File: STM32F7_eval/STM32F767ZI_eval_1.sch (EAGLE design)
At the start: 91 parts, among them CN1 GROVE-4P-CONN-I2C-90D, CN2 GROVE-4P-CONN-I2C-90D, CN3 GROVE-4P-CONN-I2C-90D, CN4 GROVE-4P-CONN-AN01-90D, CN5 ARDUINO_COMPAT_IF, CN6 STLINKV21_SWD_IF, CN7 WFT0750CZ09-SMD_, CN8 MCO_IF, CN9 UART_IF, Q1 PMF370XN_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

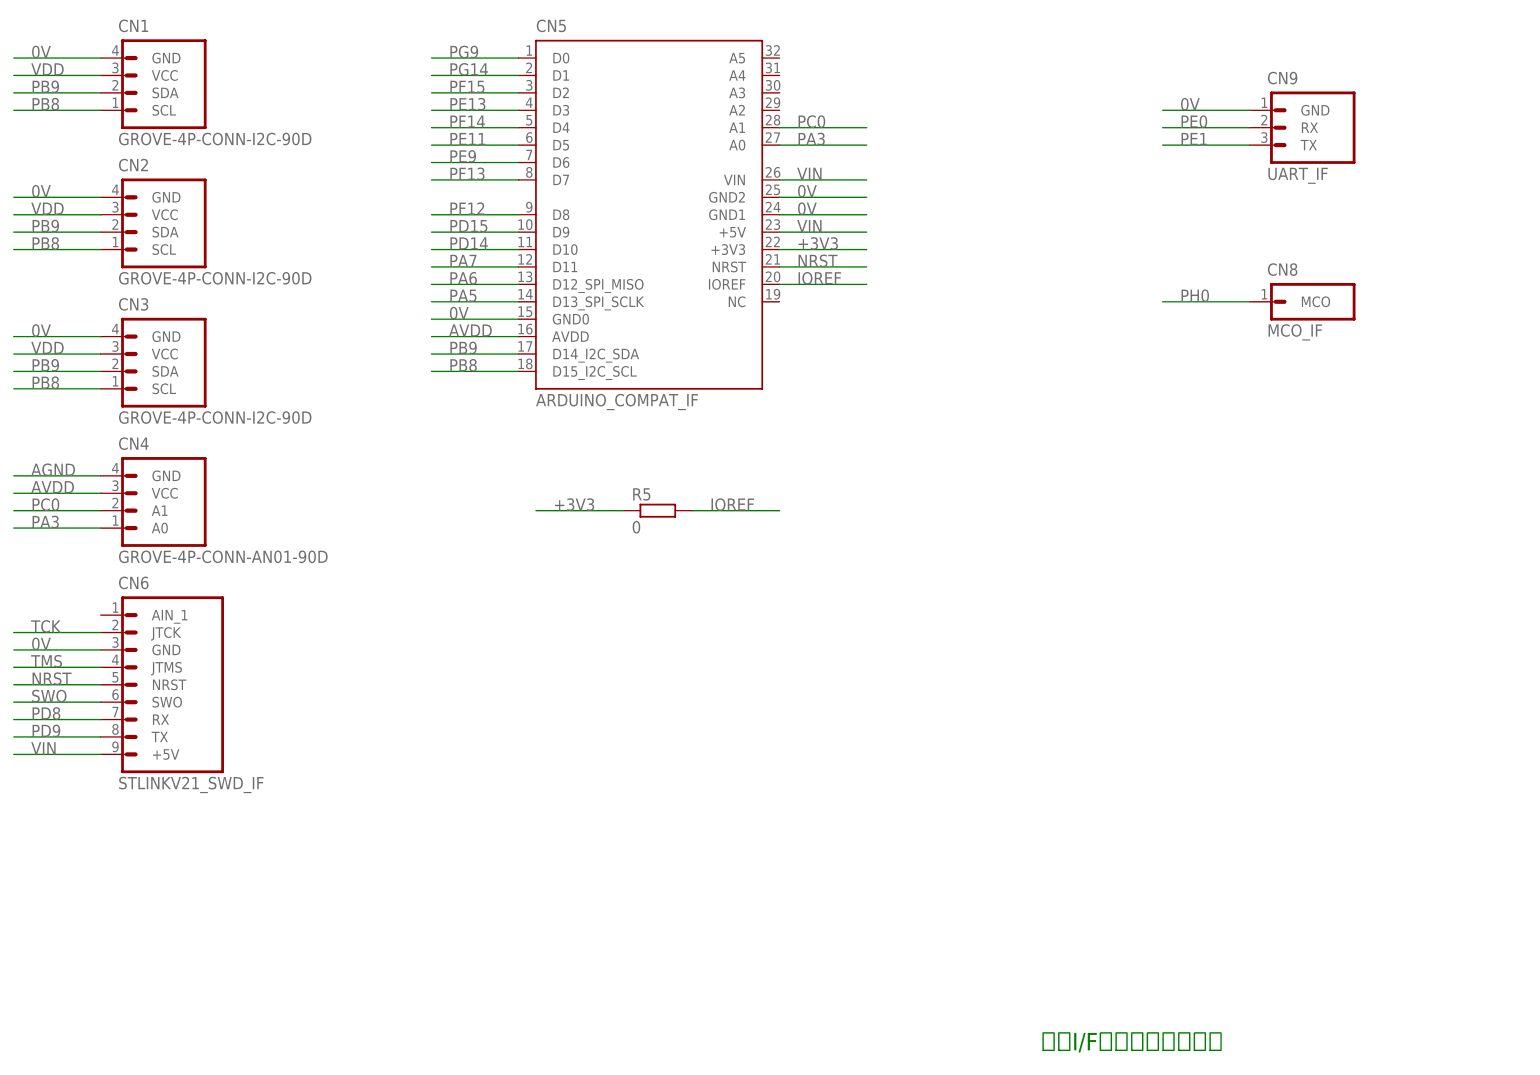
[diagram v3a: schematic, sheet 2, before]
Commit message: 評価基板を修正
・電源回路の出力側にバイパスコンデンサーを追加
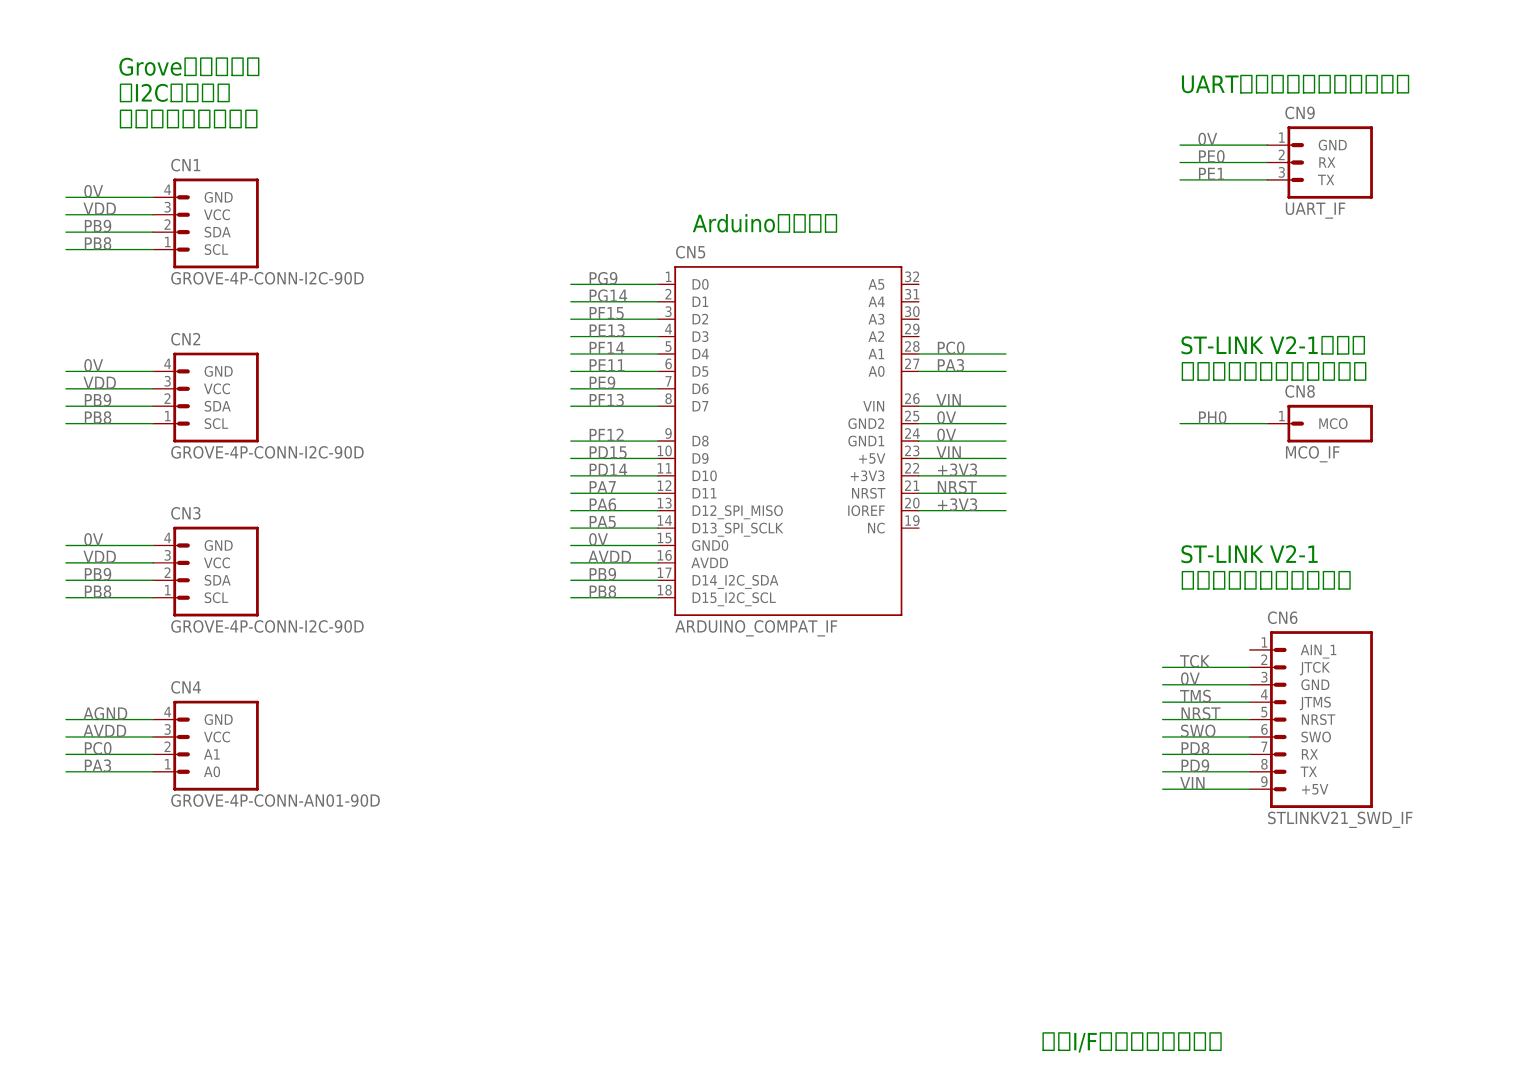
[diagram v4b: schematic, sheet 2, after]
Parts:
- removed R5: 0, Parts:RESISTOR_0603_DEV
- added C40: 1uF X5R, Parts:CAP_0603_DEV
- added C41: 0.1uF50V, Parts:CAP_0603_DEV
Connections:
- removed net IOREF: CN5.IOREF, R5.2
- net +3V3: now also C40.1, C41.1, CN5.IOREF; no longer R5.1
- net 0V: now also C40.2, C41.2
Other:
- note added: "1uF/0.1uFは LDOのVOUT近傍に設置"
- note added: "1uFは VBATの近傍に設置"
- note added: "Arduino互換ピン"
- note added: "Groveコネクター ・I2C３ポート ・アナログ１ポート"
- note added: "ST-LINK V2-1 インターフェース用ピン"
- note added: "ST-LINK V2-1からの マスタークロック入力ピン"
- note added: "UARTインターフェース用ピン"
- moved on the sheet: C19, C22, C23, CN1, CN2, CN3, CN4, CN5, CN6, CN8, CN9, FB1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

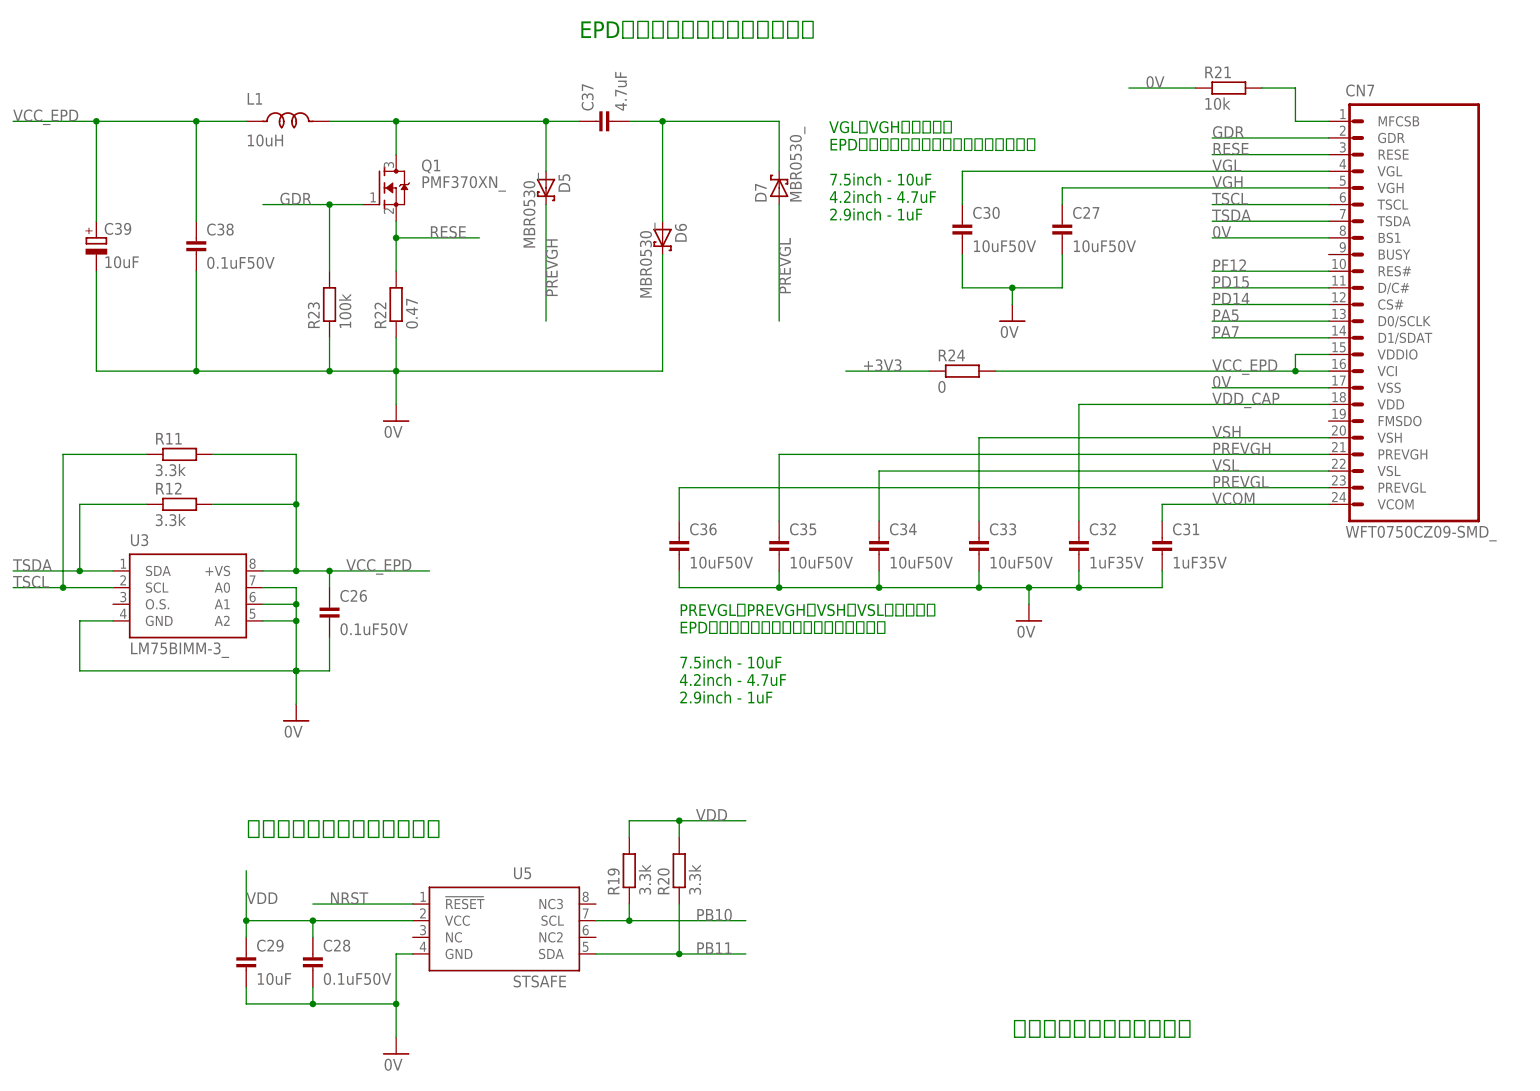
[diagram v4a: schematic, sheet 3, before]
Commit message: 評価基板を修正
・定数記述を修正
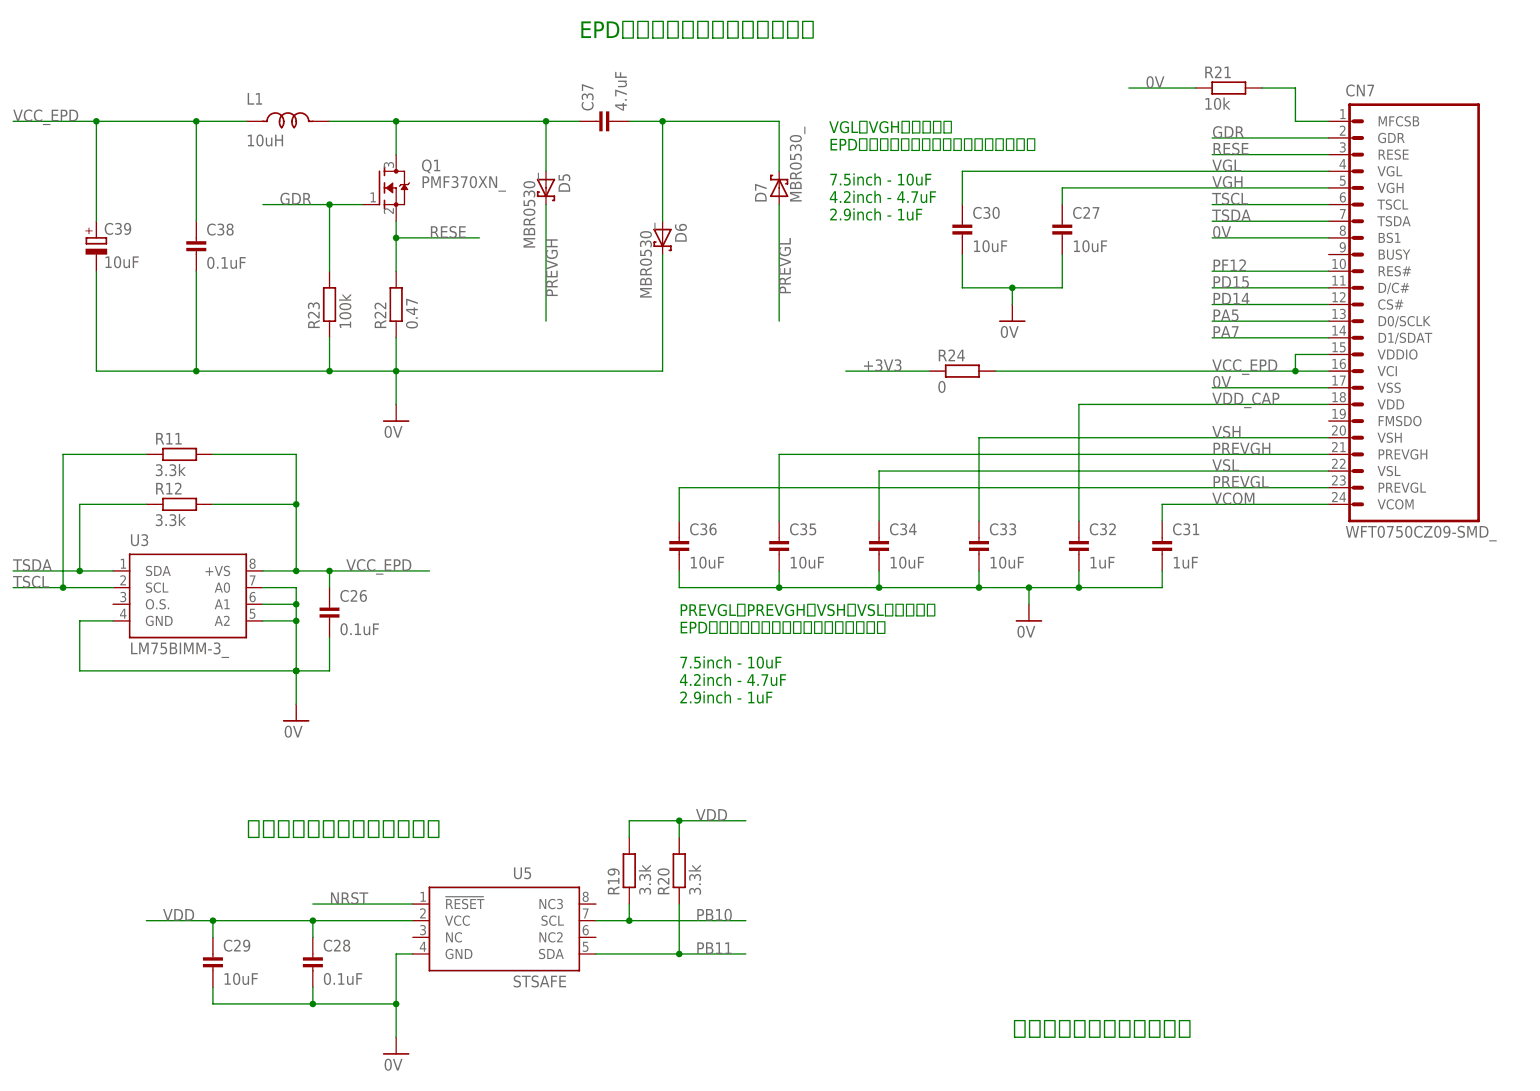
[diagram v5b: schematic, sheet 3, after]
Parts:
- C1, C10, C11, C12, C17, C18, C19, C2, C26, C28, C3, C38, C4, C41, C5, C6, C7, C8, C9: value 0.1uF50V -> 0.1uF
- C25, C31, C32: value 1uF35V -> 1uF
- C27, C30, C33, C34, C35, C36: value 10uF50V -> 10uF
- R6: value 330 -> 300
- R7: value 220k -> 200k
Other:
- moved on the sheet: C29

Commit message: 評価回路を修正
・オプションデバイス追加
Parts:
- added C42, C44, C45, C46: 0.1uF, Parts:CAP_0603_DEV
- added C43: 1uF, Parts:CAP_0603_DEV
- added R25, R26, R27, R28, R29, R30: 0, Parts:RESISTOR_0603_DEV
- added R5: 10k, Parts:RESISTOR_0603_DEV
- added U6: MX25U6435F, Parts:MX25U6435F
- added U7: AE-FXMA108, PartsForProto:AE-FXMA108
- added U8: NCP563, Parts:NCP563
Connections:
- new net !CS!: U6.!CS, U7.B1
- new net !RESET!: U6.!RESET!/SIO3, U7.B0
- new net +18V: C42.1, C44.1, C46.1, U6.!WP!/SIO2, U6.VCC, U7.VCCB, U8.VOUT
- new net CS_MEM: R27.2, U7.A1
- new net MISO_MEM: R29.2, U7.A3
- new net MOSI_MEM: R28.2, U7.A2
- new net N$15: R5.2, U7.!OE!
- new net PA15: R27.1, U1.PA15
- new net PC10: R30.1, U1.PC10
- new net PC11: R29.1, U1.PC11
- new net PC12: R28.1, U1.PC12
- new net RST_MEM: R26.2, U7.A0
- new net SCLK: U6.SCLK, U7.B4
- new net SCLK_MEM: R30.2, U7.A4
- new net SI: U6.SI/SIO0, U7.B2
- new net SO: U6.SO/SIO1, U7.B3
- new net VCC_MEM: C43.1, C45.1, R25.2, U7.VCCA, U8.VIN
- net +3V3: now also R25.1
- net 0V: now also C42.2, C43.2, C44.2, C45.2, C46.2, R5.1, U6.GND, U7.GND, U8.GND
- net NRST: now also R26.1
- net PA7: now also CN5.D11_SPI_MOSI; no longer CN5.D11
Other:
- note added: "!CS!に LOW を出力時は フラッシュが使用可能"
- note added: "!OE!に LOW を出力時は FXMA108のバスが 使用可能になる"
- note added: "!RESET!は GPIOを使用しても制御可能"
- note added: "+3V3と STM32F767ZIのSPIに ジャンパーを介し接続"
- note added: "0.1uFをVoutピンの近傍に設置 以下のいずれかを推奨： C2012X5R1C105K C1608X5R1A105K C3216X7R1C105K"
- note added: "1uFをVinピンの近傍に設置 以下のいずれかを推奨： C2012X5R1C105K C1608X5R1A105K"
- note added: "セラミックコンデンサーを VCCピンの近傍に設置"
